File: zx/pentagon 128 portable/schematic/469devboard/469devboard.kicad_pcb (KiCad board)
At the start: 4 copper layers, 77 parts, among them IC1 1072, J3 10033526-N3212LF, J4 Conn_01x03_Male, J5 Conn_01x35_Male, J6 Conn_01x36_Male, J7 Conn_01x23_Male, J8 Conn_01x30_Male, J9 104031-0811, U1 STM32F469IITx, U2 LD1117S33TR_SOT223, Y1 Q13FC1350000400, Y2 ABM3B-8.000MHZ-10-1-U-T

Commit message: updated board and notes
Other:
- board outline added: 94.6 x 98.4 mm
- board text added: "Rev. 1.00"
- board text added: "stm32f469 DevBoard"

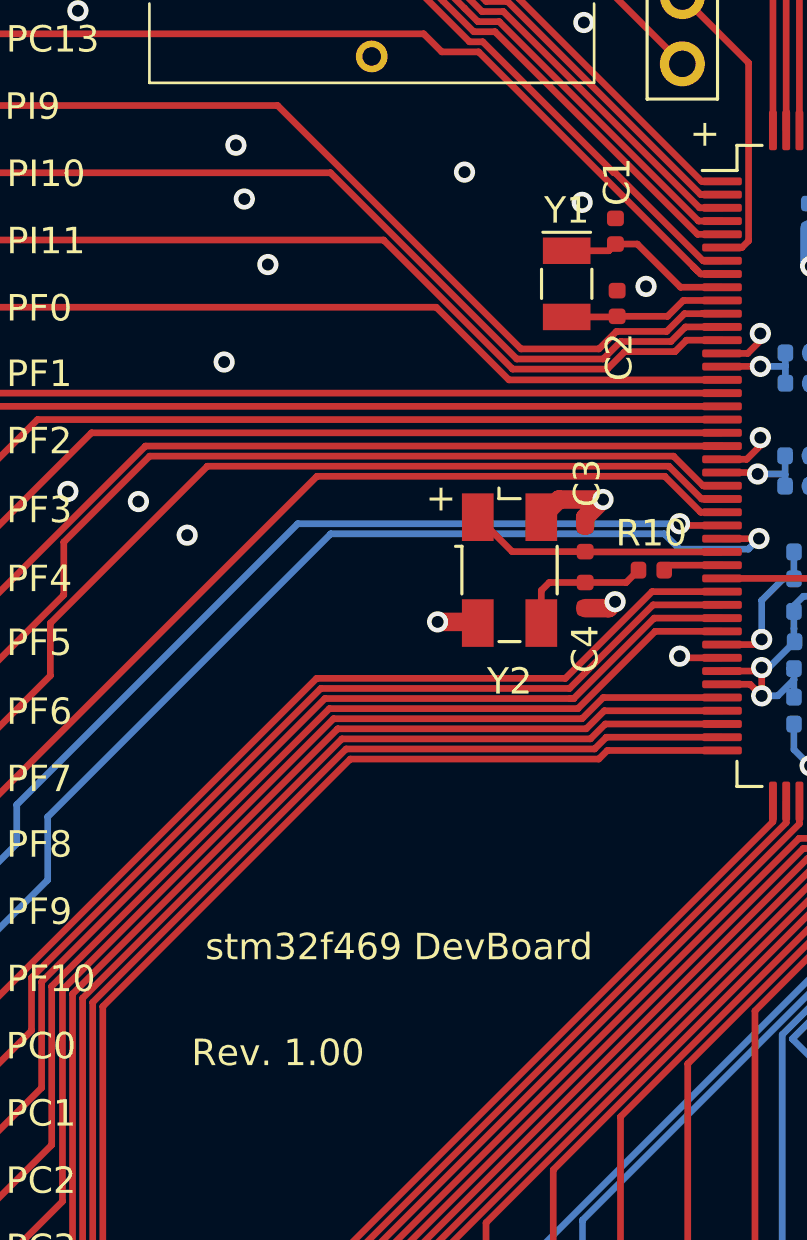
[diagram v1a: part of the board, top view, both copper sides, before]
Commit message: fixed 496 devboard
fixed tracks for oscillators
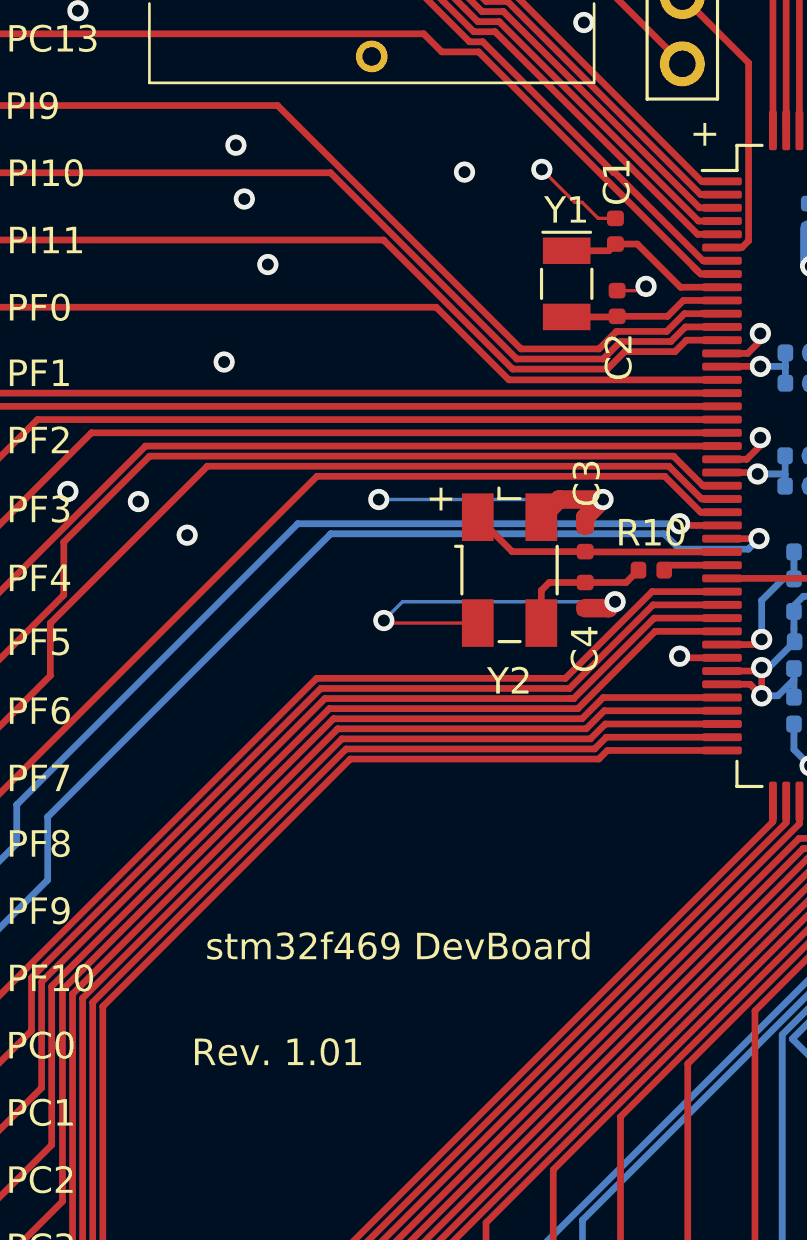
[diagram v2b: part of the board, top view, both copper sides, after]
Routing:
- net GND: track 119.5 -> 143.8 mm, vias 121 -> 122
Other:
- board text added: "Rev. 1.01"
- board text removed: "Rev. 1.00"

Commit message: pentagon
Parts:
- renumbered FMC to J1, +3.3V to J10, DSI to J11, GND to J12, JTAG to J2, RESET to SW1
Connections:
- J1 pad 9: (no net) -> /+3.3V
- J9 pad 4: (no net) -> /+3.3V
